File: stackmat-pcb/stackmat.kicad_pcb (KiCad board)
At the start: 2 copper layers, 50.6 x 33.9 mm, 14 parts, among them U2 18650, U3 AMS1117-3.3

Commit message: feat: delegate button
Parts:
- BTN1: value Conn_01x03 -> Conn_01x05; footprint Connector_PinHeader_2.54mm:PinHeader_1x03_P2.54mm_Vertical -> Connector_PinHeader_2.54mm:PinHeader_1x05_P2.54mm_Vertical
- R2: value R100000 -> R10000
- moved LCD1 3.81 mm to (93.3, 102.4)
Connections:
- BTN1 pad 2: Net-(BTN1-Pin_2) -> +3.3V
- ESP12f1 pad 16: Net-(ESP12f1-GPIO15) -> Net-(BTN1-Pin_5)
- ESP12f1 pad 17: Net-(BTN1-Pin_2) -> Net-(BTN1-Pin_3)
- ESP12f1 pad 18: Net-(BTN1-Pin_3) -> Net-(BTN1-Pin_4)
- ESP12f1 pad 4: unconnected-(ESP12f1-GPIO16-Pad4) -> Net-(ESP12f1-GPIO16)
- R1 pad 1: Net-(ESP12f1-GPIO15) -> Net-(BTN1-Pin_5)
- RFID1 pad 3: Net-(ESP12f1-GPIO15) -> Net-(ESP12f1-GPIO16)
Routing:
- net Net-(ESP12f1-GPIO15): track 27.0 -> 0.00 mm, vias 1 -> 0
- net Net-(ESP12f1-GPIO16): track 0.00 -> 26.4 mm, vias 0 -> 3
- net Net-(BTN1-Pin_5): track 0.00 -> 20.2 mm, vias 0 -> 1
- net Net-(BTN1-Pin_4): track 0.00 -> 13.4 mm, vias 0 -> 1
- net Net-(BTN1-Pin_2): track 11.6 -> 0.00 mm, vias 1 -> 0
- net +3.3V: track 59.9 -> 64.4 mm
- net Net-(BTN1-Pin_3): track 13.0 -> 9.93 mm
- net Net-(ESP12f1-GPIO4): track 18.7 -> 20.3 mm
- net Net-(ESP12f1-GPIO5): track 23.7 -> 25.3 mm
- net Net-(ESP12f1-GPIO14): track 33.2 -> 34.0 mm
- net Net-(ESP12f1-GPIO12): track 27.5 -> 28.3 mm
- net Net-(ESP12f1-GPIO13): track 21.0 -> 21.8 mm

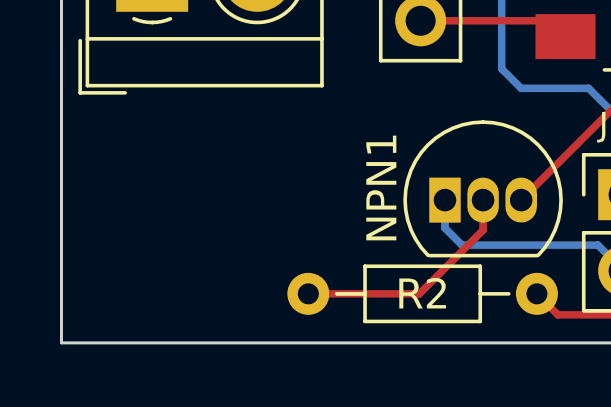
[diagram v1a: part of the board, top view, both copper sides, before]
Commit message: chore: mousebites for panel (2x1 because jlcpcb was mad)
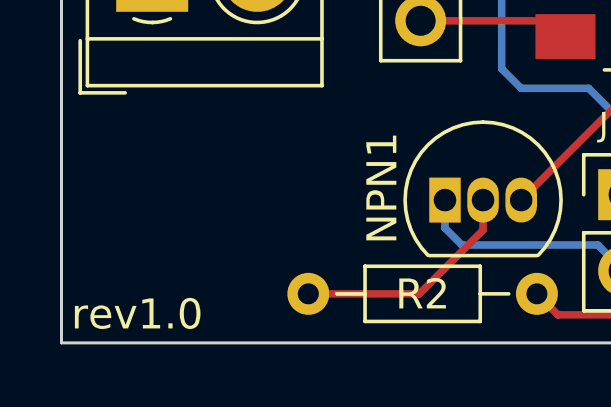
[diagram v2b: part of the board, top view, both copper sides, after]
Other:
- board text added: "rev1.0"
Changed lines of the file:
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@@
   (gr_rect (start 66.502 74.63) (end 117.102 108.56)
     (stroke (width 0.1) (type default)) (fill none) (layer "Edge.Cuts"))
+  (gr_text "rev1.0" (at 66.825 108.2) (layer "F.SilkS")
+    (effects (font (size 1 1) (thickness 0.15)) (justify left bottom))
+  )
   (segment (start 114.77 106.215) (end 114.83 106.275) (width 0.25) (layer "F.Cu") (net 1))
   (segment (start 85.06 103.8) (end 85.24 103.62) (width 0.25) (layer "F.Cu") (net 1))

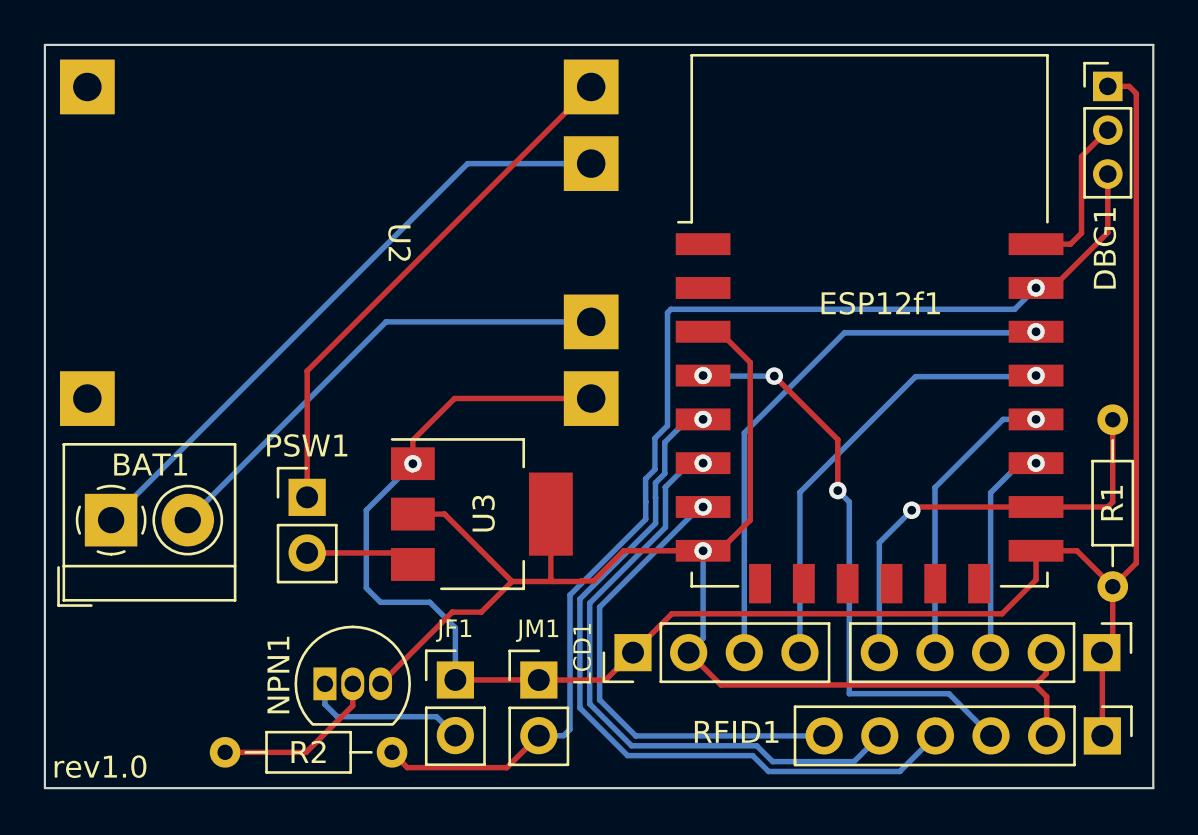
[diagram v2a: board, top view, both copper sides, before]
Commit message: chore: smaller board (smallest i could do without changing layout) - so panelized is 102x102mm (2USD on jlcpcb)
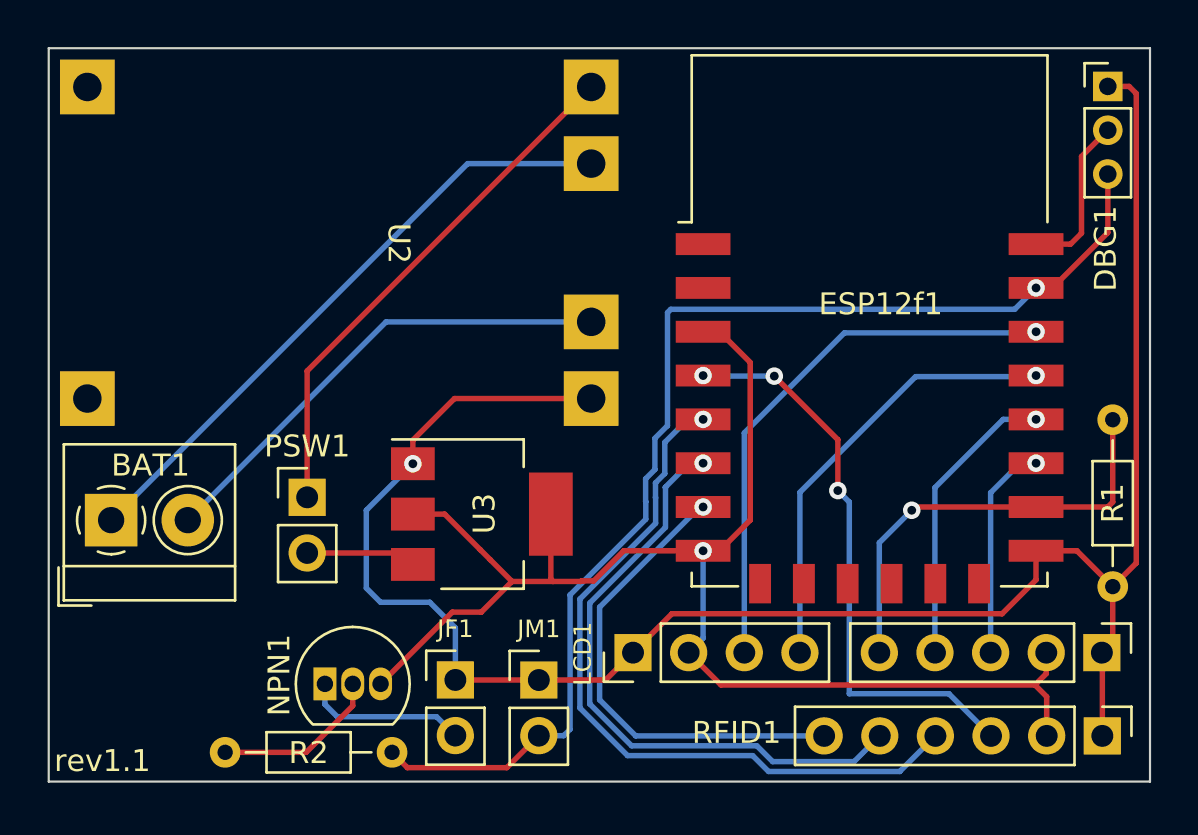
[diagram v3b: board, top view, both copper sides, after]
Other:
- board size 50.6 x 33.9 mm -> 50.3 x 33.5 mm
- board text added: "rev1.1"
- board text removed: "rev1.0"
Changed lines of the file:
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@@
   (gr_line (start 73.002981 80.625) (end 72.354132 80.625)
     (stroke (width 0.239863) (type solid)) (layer "B.SilkS"))
-  (gr_rect (start 66.502 74.63) (end 117.102 108.56)
+  (gr_rect (start 66.677 74.78) (end 116.952 108.26)
     (stroke (width 0.1) (type default)) (fill none) (layer "Edge.Cuts"))
-  (gr_text "rev1.0" (at 66.825 108.2) (layer "F.SilkS")
+  (gr_text "rev1.1" (at 66.925 107.9) (layer "F.SilkS")
     (effects (font (size 1 1) (thickness 0.15)) (justify left bottom))
   )

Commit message: fix: lcd 5v instead of 3.3v
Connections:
- LCD1 pad 2: +3.3V -> +5V
- PSW1 pad 2: Net-(PSW1-Pin_2) -> +5V
- U3 pad 3: Net-(PSW1-Pin_2) -> +5V
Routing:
- net +5V: track 0.00 -> 19.3 mm, vias 0 -> 3
- net Net-(PSW1-Pin_2): track 5.04 -> 0.00 mm
- net +3.3V: track 64.4 -> 63.8 mm, vias 1 -> 2

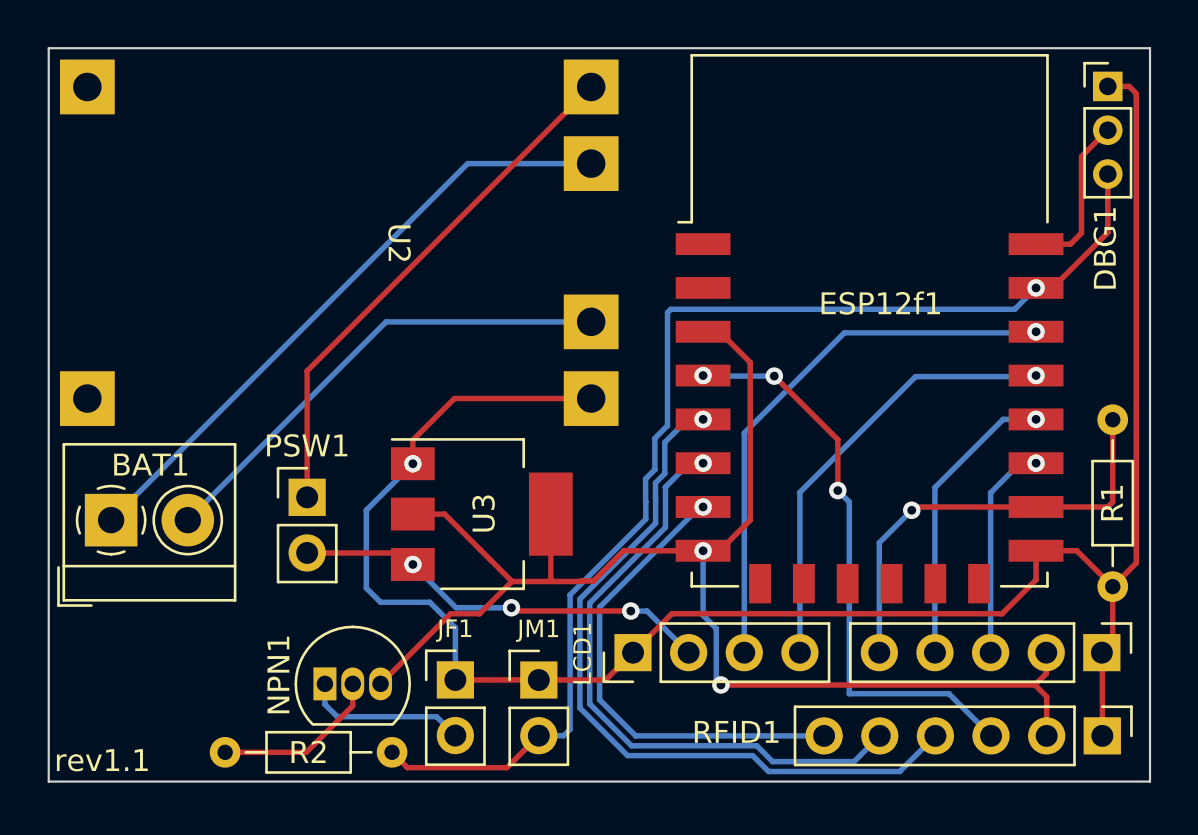
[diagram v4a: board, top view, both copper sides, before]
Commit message: feat: better pcb debug pins
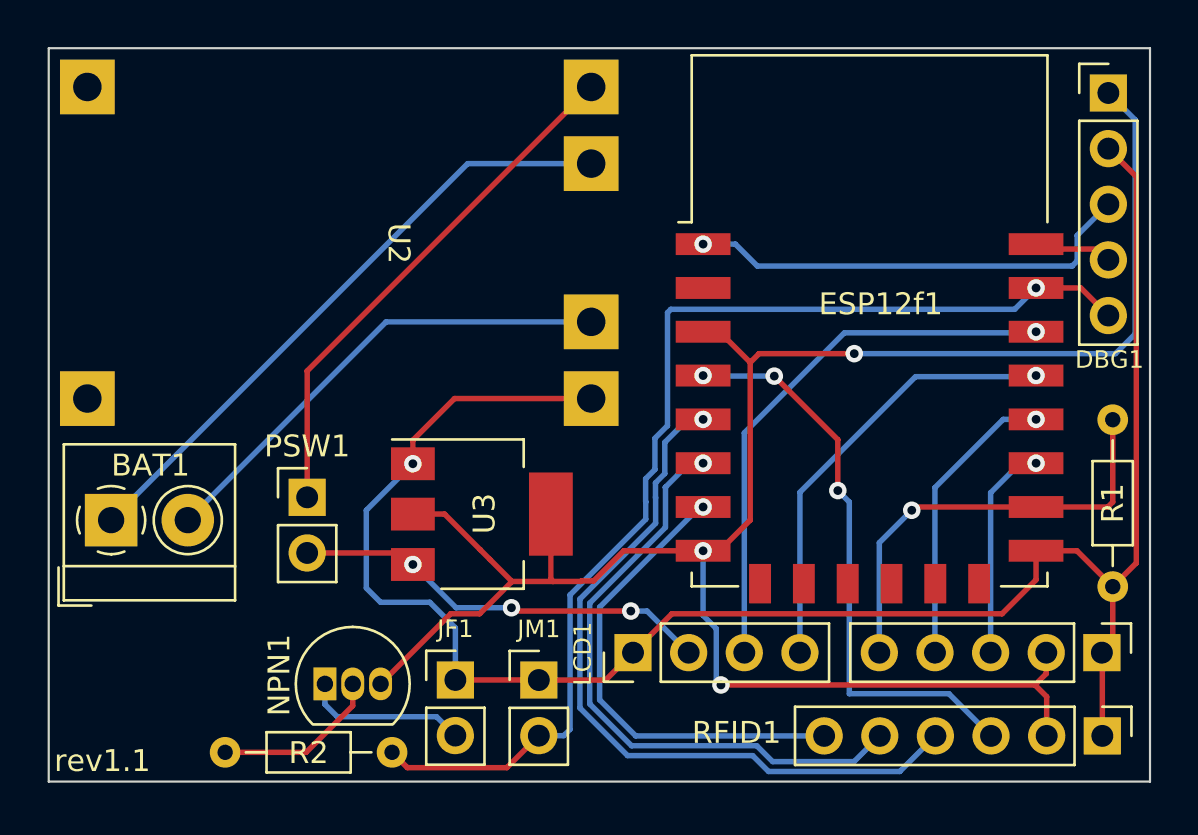
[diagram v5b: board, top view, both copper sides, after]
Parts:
- DBG1: value DBG_SERIAL -> Conn_01x05; footprint Connector_PinHeader_2.00mm:PinHeader_1x03_P2.00mm_Vertical -> Connector_PinHeader_2.54mm:PinHeader_1x05_P2.54mm_Vertical
- moved DBG1 0.30 mm to (115.0, 76.8)
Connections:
- DBG1 pad 1: GND -> +3.3V
- DBG1 pad 2: Net-(DBG1-Pin_2) -> GND
- ESP12f1 pad 1: unconnected-(ESP12f1-~{RST}-Pad1) -> Net-(DBG1-Pin_3)
- ESP12f1 pad 21: Net-(DBG1-Pin_3) -> Net-(DBG1-Pin_5)
- ESP12f1 pad 22: Net-(DBG1-Pin_2) -> Net-(DBG1-Pin_4)
- JM1 pad 2: Net-(DBG1-Pin_3) -> Net-(DBG1-Pin_5)
- R2 pad 2: Net-(DBG1-Pin_3) -> Net-(DBG1-Pin_5)
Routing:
- net Net-(DBG1-Pin_5): track 0.00 -> 51.1 mm, vias 0 -> 1
- net Net-(DBG1-Pin_3): track 54.3 -> 20.8 mm
- net +3.3V: track 63.8 -> 93.5 mm, vias 2 -> 3
- net Net-(DBG1-Pin_2): track 8.23 -> 0.00 mm
- net Net-(DBG1-Pin_4): track 0.00 -> 4.35 mm
- net GND: track 89.4 -> 86.0 mm
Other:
- board text added: "DBG1"

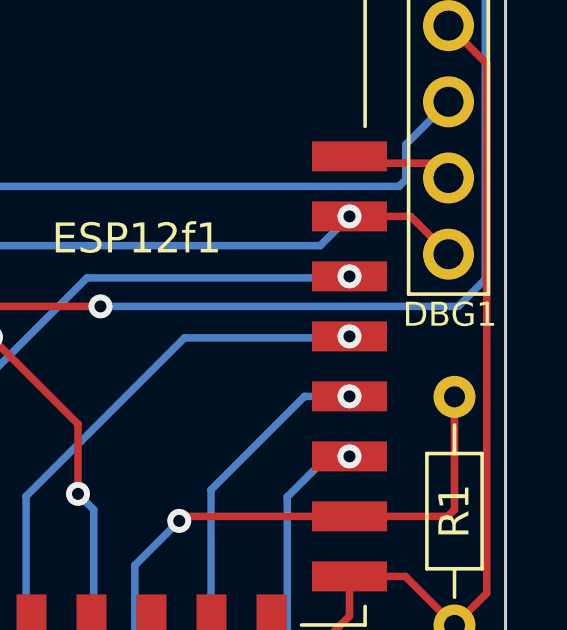
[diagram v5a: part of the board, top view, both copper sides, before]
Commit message: feat: lcd printf helper (with aligments etc)
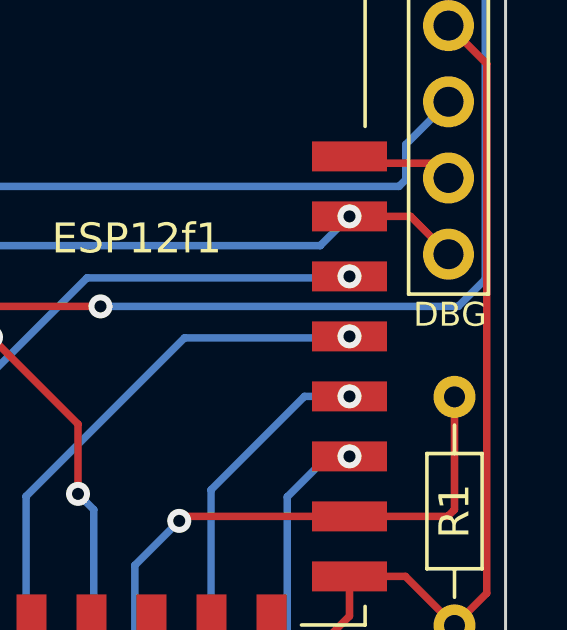
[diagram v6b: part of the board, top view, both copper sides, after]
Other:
- board text added: "DBG"
- board text removed: "DBG1"
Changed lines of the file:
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@@
     (effects (font (size 1 1) (thickness 0.15)) (justify left bottom))
   )
-  (gr_text "DBG1" (at 115.1 89) (layer "F.SilkS")
+  (gr_text "DBG" (at 115.1 89) (layer "F.SilkS")
     (effects (font (size 0.8 0.8) (thickness 0.15)))
   )
